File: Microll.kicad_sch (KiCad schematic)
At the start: 3 parts

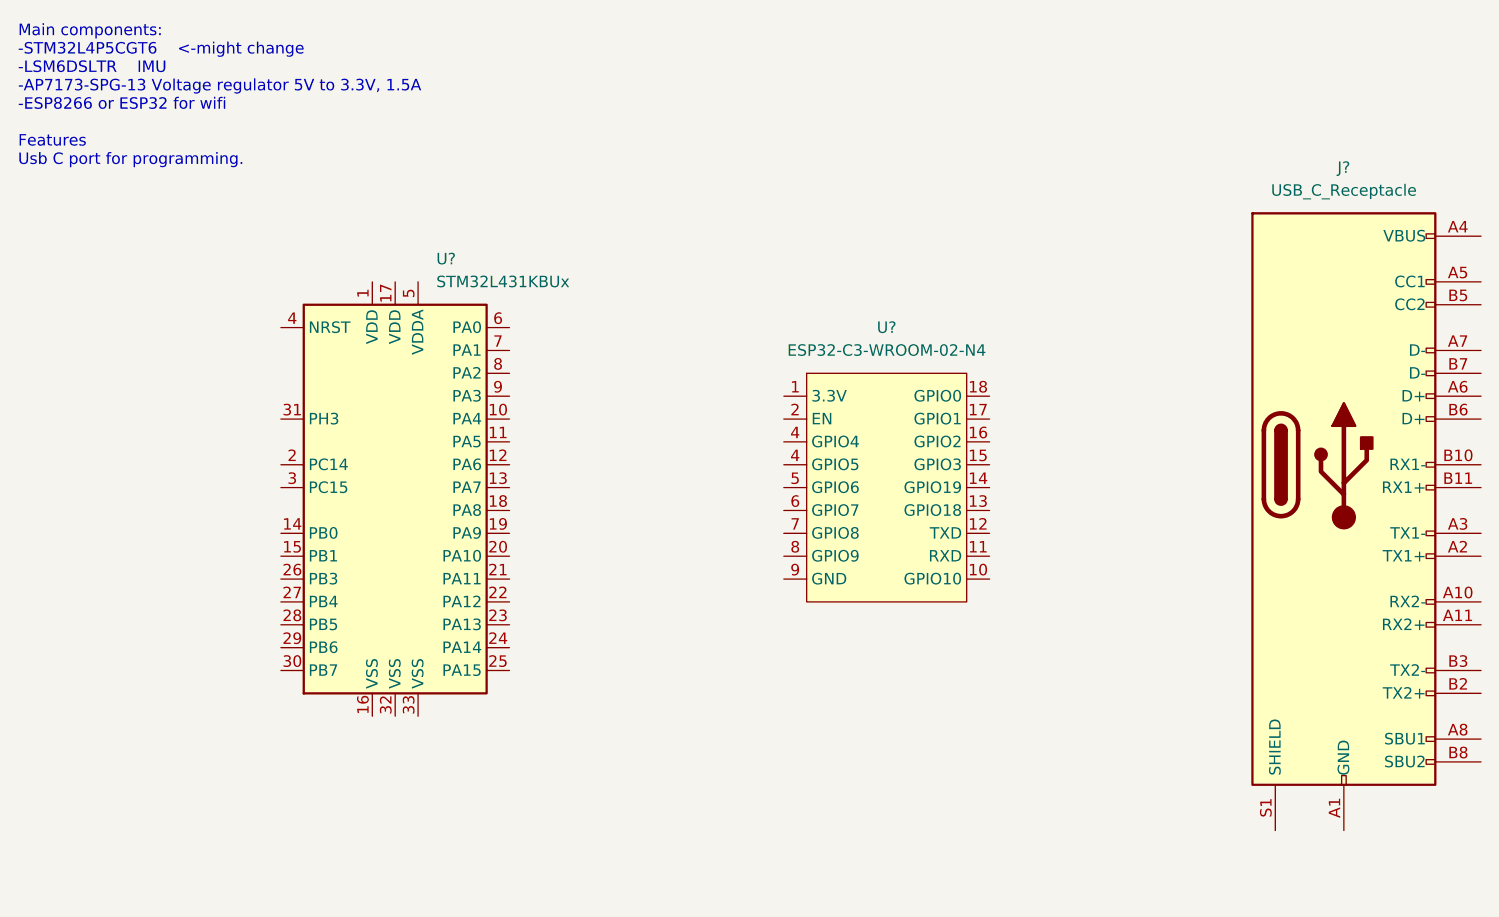
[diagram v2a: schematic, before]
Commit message: Added linear regulator symbol and footprint.
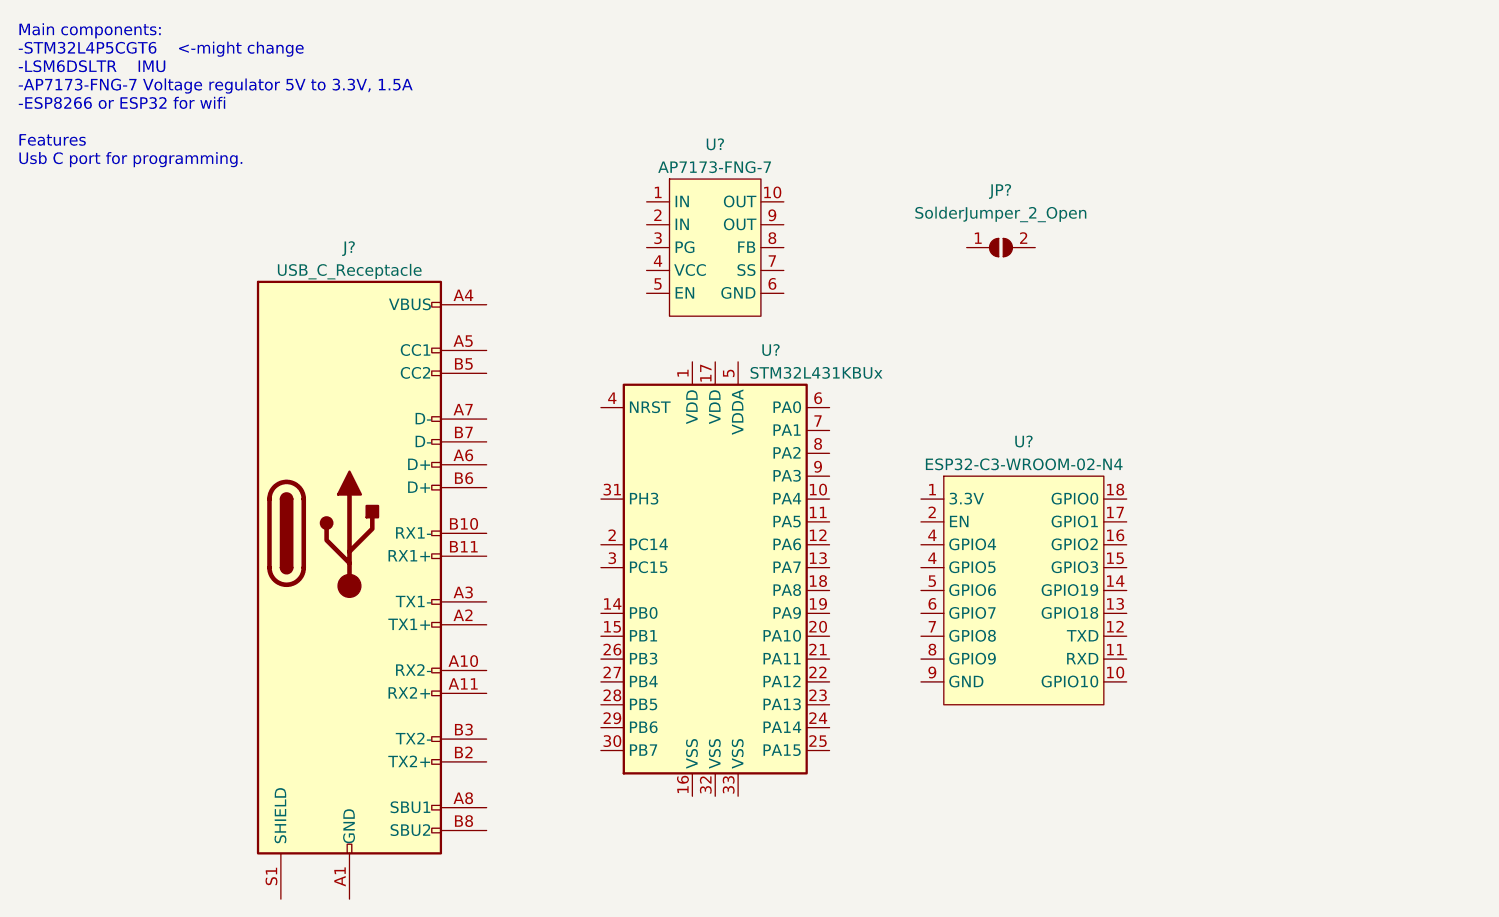
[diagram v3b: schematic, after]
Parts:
- added JP?: SolderJumper_2_Open, symbol Jumper:SolderJumper_2_Open
- added U?: AP7173-FNG-7, AP7173-FNG-7:AP7173-FNG-7, symbol AP7173-FNG-7:AP7173-FNG-7
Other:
- note added: "Main components: -STM32L4P5CGT6 <-might change -LSM6DSLTR IMU -AP7173-FNG-7 Voltage regulator 5V to 3.3V, 1.5A -ESP8266 or ESP32 for wifi Features Usb C port for programming."
- note removed: "Main components: -STM32L4P5CGT6 <-might change -LSM6DSLTR IMU -AP7173-SPG-13 Voltage regulator 5V to 3.3V, 1.5A -ESP8266 or ESP32 for wifi Features Usb C port for programming."
- moved on the sheet: J?, U?
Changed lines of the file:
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@@
 (kicad_sch (version 20211123) (generator eeschema)
   (paper "A4")
-  (text "Main components:\n-STM32L4P5CGT6	<-might change	\n-LSM6DSLTR	IMU\n-AP7173-SPG-13 Voltage regulator 5V to 3.3V, 1.5A\n-ESP8266 or ESP32 for wifi\n\nFeatures\nUsb C port for programming."
+  (text "Main components:\n-STM32L4P5CGT6	<-might change	\n-LSM6DSLTR	IMU\n-AP7173-FNG-7 Voltage regulator 5V to 3.3V, 1.5A\n-ESP8266 or ESP32 for wifi\n\nFeatures\nUsb C port for programming."
     (at 59.69 50.8 0)
     (effects (font (size 1.27 1.27)) (justify left bottom))
   )
-  (symbol (lib_id "MCU_ST_STM32L4:STM32L431KBUx") (at 101.6 86.36 0) (unit 1)
-    (in_bom yes) (on_board yes) (fields_autoplaced)
-    (property "Reference" "U?" (id 0) (at 106.1594 60.96 0)
+  (symbol (lib_id "MCU_ST_STM32L4:STM32L431KBUx") (at 137.16 95.25 0) (unit 1)
+    (in_bom yes) (on_board yes)
+    (property "Reference" "U?" (id 0) (at 142.24 71.12 0)
       (effects (font (size 1.27 1.27)) (justify left))
     )
-    (property "Value" "STM32L431KBUx" (id 1) (at 106.1594 63.5 0)
+    (property "Value" "STM32L431KBUx" (id 1) (at 140.97 73.66 0)
       (effects (font (size 1.27 1.27)) (justify left))
     )
-    (property "Footprint" "Package_DFN_QFN:QFN-32-1EP_5x5mm_P0.5mm_EP3.45x3.45mm" (id 2) (at 91.44 109.22 0)
+    (property "Footprint" "Package_DFN_QFN:QFN-32-1EP_5x5mm_P0.5mm_EP3.45x3.45mm" (id 2) (at 127 118.11 0)
       (effects (font (size 1.27 1.27)) (justify right) hide)
     )
-    (property "Datasheet" "http://www.st.com/st-web-ui/static/active/en/resource/technical/document/datasheet/DM00257211.pdf" (id 3) (at 101.6 86.36 0)
+    (property "Datasheet" "http://www.st.com/st-web-ui/static/active/en/resource/technical/document/datasheet/DM00257211.pdf" (id 3) (at 137.16 95.25 0)
       (effects (font (size 1.27 1.27)) hide)
     )
@@
     (pin "9")
   )
-  (symbol (lib_id "ESP32:ESP32-C3-WROOM-02-N4") (at 156.21 82.55 0) (unit 1)
+  (symbol (lib_id "Jumper:SolderJumper_2_Open") (at 168.91 59.69 0) (unit 1)
     (in_bom yes) (on_board yes) (fields_autoplaced)
-    (property "Reference" "U?" (id 0) (at 156.21 68.58 0))
-    (property "Value" "ESP32-C3-WROOM-02-N4" (id 1) (at 156.21 71.12 0))
-    (property "Footprint" "ESP32:ESP32-C3-WROOM-02-N4" (id 2) (at 156.21 82.55 0)
+    (property "Reference" "JP?" (id 0) (at 168.91 53.34 0))
+    (property "Value" "SolderJumper_2_Open" (id 1) (at 168.91 55.88 0))
+    (property "Footprint" "" (id 2) (at 168.91 59.69 0)
       (effects (font (size 1.27 1.27)) hide)
     )
-    (property "Datasheet" "" (id 3) (at 156.21 82.55 0)
+    (property "Datasheet" "~" (id 3) (at 168.91 59.69 0)
+      (effects (font (size 1.27 1.27)) hide)
+    )
+    (pin "1")
+    (pin "2")
+  )
+  (symbol (lib_id "ESP32:ESP32-C3-WROOM-02-N4") (at 171.45 93.98 0) (unit 1)
+    (in_bom yes) (on_board yes)
+    (property "Reference" "U?" (id 0) (at 171.45 81.28 0))
+    (property "Value" "ESP32-C3-WROOM-02-N4" (id 1) (at 171.45 83.82 0))
+    (property "Footprint" "ESP32:ESP32-C3-WROOM-02-N4" (id 2) (at 171.45 93.98 0)
+      (effects (font (size 1.27 1.27)) hide)
+    )
+    (property "Datasheet" "" (id 3) (at 171.45 93.98 0)
       (effects (font (size 1.27 1.27)) hide)
     )
@@
     (pin "9")
   )
-  (symbol (lib_id "Connector:USB_C_Receptacle") (at 207.01 83.82 0) (unit 1)
-    (in_bom yes) (on_board yes) (fields_autoplaced)
-    (property "Reference" "J?" (id 0) (at 207.01 50.8 0))
-    (property "Value" "USB_C_Receptacle" (id 1) (at 207.01 53.34 0))
-    (property "Footprint" "" (id 2) (at 210.82 83.82 0)
+  (symbol (lib_id "AP7173-FNG-7:AP7173-FNG-7") (at 137.16 57.15 0) (unit 1)
+    (in_bom yes) (on_board yes)
+    (property "Reference" "U?" (id 0) (at 137.16 48.26 0))
+    (property "Value" "AP7173-FNG-7" (id 1) (at 137.16 50.8 0))
+    (property "Footprint" "AP7173-FNG-7:AP7173-FNG-7" (id 2) (at 135.89 57.15 0)
       (effects (font (size 1.27 1.27)) hide)
     )
-    (property "Datasheet" "https://www.usb.org/sites/default/files/documents/usb_type-c.zip" (id 3) (at 210.82 83.82 0)
+    (property "Datasheet" "" (id 3) (at 135.89 57.15 0)
+      (effects (font (size 1.27 1.27)) hide)
+    )
+    (pin "1")
+    (pin "10")
+    (pin "2")
+    (pin "3")
+    (pin "4")
+    (pin "5")
+    (pin "6")
+    (pin "7")
+    (pin "8")
+    (pin "9")
+  )
+  (symbol (lib_id "Connector:USB_C_Receptacle") (at 96.52 91.44 0) (unit 1)
+    (in_bom yes) (on_board yes)
+    (property "Reference" "J?" (id 0) (at 96.52 59.69 0))
+    (property "Value" "USB_C_Receptacle" (id 1) (at 96.52 62.23 0))
+    (property "Footprint" "" (id 2) (at 100.33 91.44 0)
+      (effects (font (size 1.27 1.27)) hide)
+    )
+    (property "Datasheet" "https://www.usb.org/sites/default/files/documents/usb_type-c.zip" (id 3) (at 100.33 91.44 0)
       (effects (font (size 1.27 1.27)) hide)
     )
@@
       (reference "J?") (unit 1) (value "USB_C_Receptacle") (footprint "")
     )
+    (path "/1c3b70c8-9878-40e4-8a0a-63d34ffadd04"
+      (reference "JP?") (unit 1) (value "SolderJumper_2_Open") (footprint "")
+    )
     (path "/086be992-52ad-4b7c-be4a-eeec54e5d292"
       (reference "U?") (unit 1) (value "STM32L431KBUx") (footprint "Package_DFN_QFN:QFN-32-1EP_5x5mm_P0.5mm_EP3.45x3.45mm")
@@
       (reference "U?") (unit 1) (value "ESP32-C3-WROOM-02-N4") (footprint "ESP32:ESP32-C3-WROOM-02-N4")
     )
+    (path "/52ee2e49-a114-4de8-9329-acacfc8b62fc"
+      (reference "U?") (unit 1) (value "AP7173-FNG-7") (footprint "AP7173-FNG-7:AP7173-FNG-7")
+    )
   )

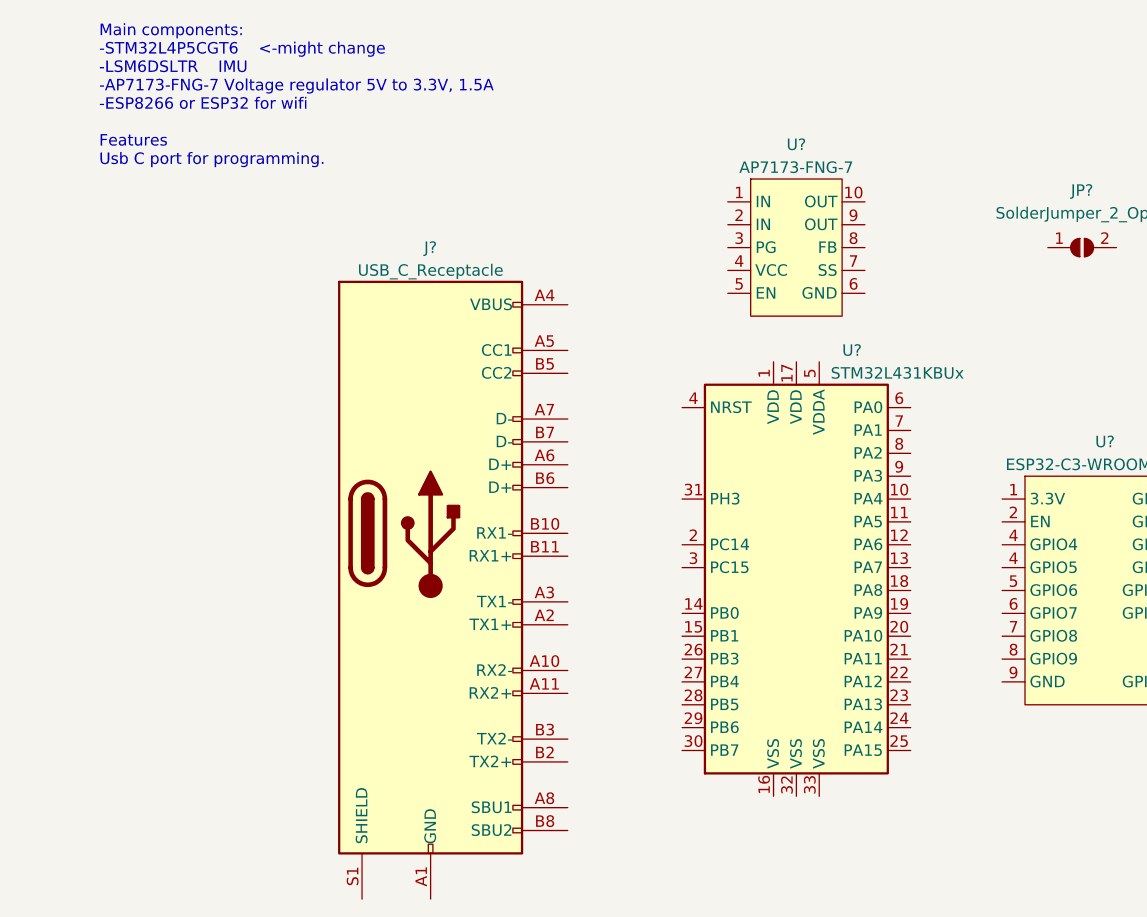
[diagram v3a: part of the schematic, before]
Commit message: Decided on STM32 microcontroller and made footprint and symbol
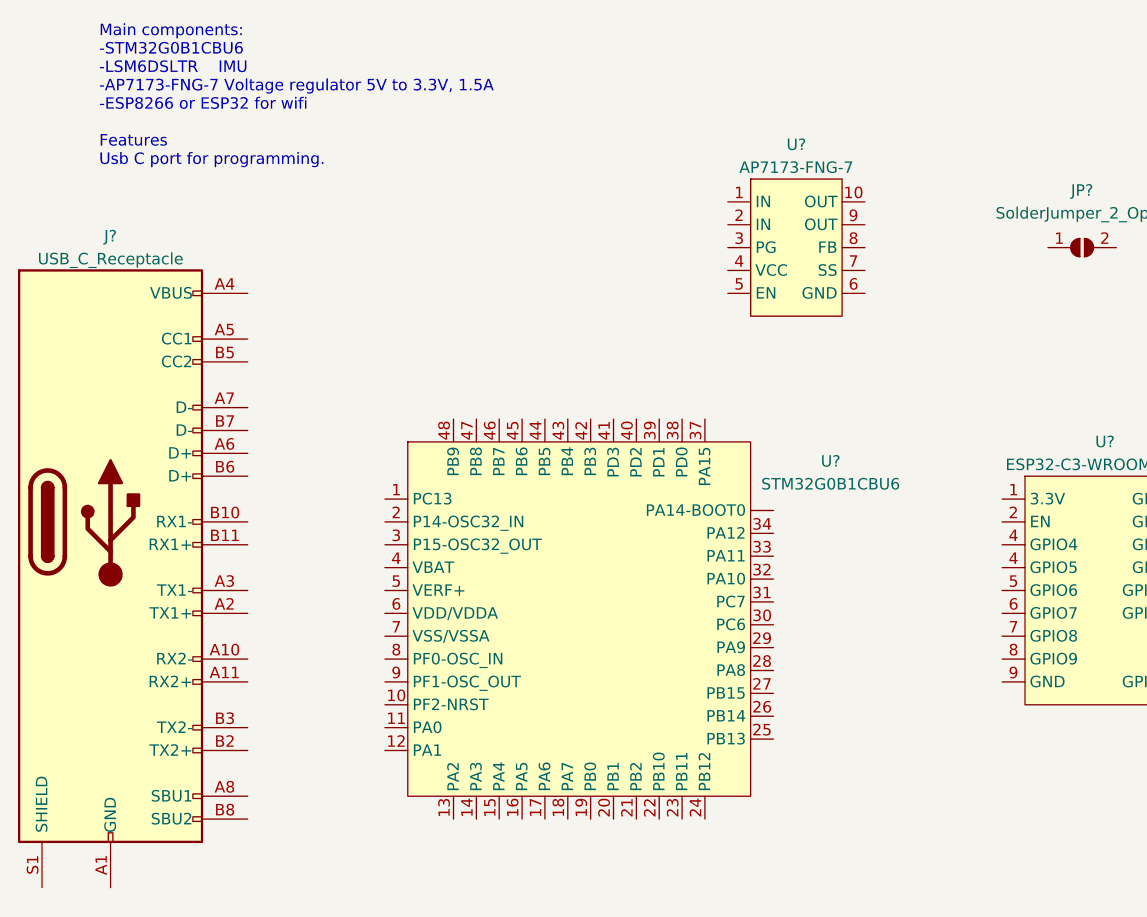
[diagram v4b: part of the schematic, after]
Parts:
- removed U?: STM32L431KBUx, Package_DFN_QFN:QFN-32-1EP_5x5mm_P0.5mm_EP3.45x3.45mm, symbol MCU_ST_STM32L4:STM32L431KBUx
- added U?: STM32G0B1CBU6, STM32:STM32G0B1CBU6, symbol STM32:STM32G0B1CBU6
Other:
- note added: "Main components: -STM32G0B1CBU6 -LSM6DSLTR IMU -AP7173-FNG-7 Voltage regulator 5V to 3.3V, 1.5A -ESP8266 or ESP32 for wifi Features Usb C port for programming."
- note removed: "Main components: -STM32L4P5CGT6 <-might change -LSM6DSLTR IMU -AP7173-FNG-7 Voltage regulator 5V to 3.3V, 1.5A -ESP8266 or ESP32 for wifi Features Usb C port for programming."
- moved on the sheet: J?
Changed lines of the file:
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@@
 (kicad_sch (version 20211123) (generator eeschema)
   (paper "A4")
-  (text "Main components:\n-STM32L4P5CGT6	<-might change	\n-LSM6DSLTR	IMU\n-AP7173-FNG-7 Voltage regulator 5V to 3.3V, 1.5A\n-ESP8266 or ESP32 for wifi\n\nFeatures\nUsb C port for programming."
+  (text "Main components:\n-STM32G0B1CBU6	\n-LSM6DSLTR	IMU\n-AP7173-FNG-7 Voltage regulator 5V to 3.3V, 1.5A\n-ESP8266 or ESP32 for wifi\n\nFeatures\nUsb C port for programming."
     (at 59.69 50.8 0)
     (effects (font (size 1.27 1.27)) (justify left bottom))
-  )
-  (symbol (lib_id "MCU_ST_STM32L4:STM32L431KBUx") (at 137.16 95.25 0) (unit 1)
-    (in_bom yes) (on_board yes)
-    (property "Reference" "U?" (id 0) (at 142.24 71.12 0)
-      (effects (font (size 1.27 1.27)) (justify left))
-    )
-    (property "Value" "STM32L431KBUx" (id 1) (at 140.97 73.66 0)
-      (effects (font (size 1.27 1.27)) (justify left))
-    )
-    (property "Footprint" "Package_DFN_QFN:QFN-32-1EP_5x5mm_P0.5mm_EP3.45x3.45mm" (id 2) (at 127 118.11 0)
-      (effects (font (size 1.27 1.27)) (justify right) hide)
-    )
-    (property "Datasheet" "http://www.st.com/st-web-ui/static/active/en/resource/technical/document/datasheet/DM00257211.pdf" (id 3) (at 137.16 95.25 0)
-      (effects (font (size 1.27 1.27)) hide)
-    )
-    (pin "1")
-    (pin "10")
-    (pin "11")
-    (pin "12")
-    (pin "13")
-    (pin "14")
-    (pin "15")
-    (pin "16")
-    (pin "17")
-    (pin "18")
-    (pin "19")
-    (pin "2")
-    (pin "20")
-    (pin "21")
-    (pin "22")
-    (pin "23")
-    (pin "24")
-    (pin "25")
-    (pin "26")
-    (pin "27")
-    (pin "28")
-    (pin "29")
-    (pin "3")
-    (pin "30")
-    (pin "31")
-    (pin "32")
-    (pin "33")
-    (pin "4")
-    (pin "5")
-    (pin "6")
-    (pin "7")
-    (pin "8")
-    (pin "9")
   )
   (symbol (lib_id "Jumper:SolderJumper_2_Open") (at 168.91 59.69 0) (unit 1)
@@
     (pin "9")
   )
+  (symbol (lib_id "STM32:STM32G0B1CBU6") (at 113.03 101.6 0) (unit 1)
+    (in_bom yes) (on_board yes) (fields_autoplaced)
+    (property "Reference" "U?" (id 0) (at 140.97 83.4388 0))
+    (property "Value" "STM32G0B1CBU6" (id 1) (at 140.97 85.9788 0))
+    (property "Footprint" "STM32:STM32G0B1CBU6" (id 2) (at 105.41 92.71 0)
+      (effects (font (size 1.27 1.27)) hide)
+    )
+    (property "Datasheet" "" (id 3) (at 105.41 92.71 0)
+      (effects (font (size 1.27 1.27)) hide)
+    )
+    (pin "")
+    (pin "1")
+    (pin "10")
+    (pin "11")
+    (pin "12")
+    (pin "13")
+    (pin "14")
+    (pin "15")
+    (pin "16")
+    (pin "17")
+    (pin "18")
+    (pin "19")
+    (pin "2")
+    (pin "20")
+    (pin "21")
+    (pin "22")
+    (pin "23")
+    (pin "24")
+    (pin "25")
+    (pin "26")
+    (pin "27")
+    (pin "28")
+    (pin "29")
+    (pin "3")
+    (pin "30")
+    (pin "31")
+    (pin "32")
+    (pin "33")
+    (pin "34")
+    (pin "37")
+    (pin "38")
+    (pin "39")
+    (pin "4")
+    (pin "40")
+    (pin "41")
+    (pin "42")
+    (pin "43")
+    (pin "44")
+    (pin "45")
+    (pin "46")
+    (pin "47")
+    (pin "48")
+    (pin "5")
+    (pin "6")
+    (pin "7")
+    (pin "8")
+    (pin "9")
+  )
   (symbol (lib_id "AP7173-FNG-7:AP7173-FNG-7") (at 137.16 57.15 0) (unit 1)
     (in_bom yes) (on_board yes)
@@
     (pin "9")
   )
-  (symbol (lib_id "Connector:USB_C_Receptacle") (at 96.52 91.44 0) (unit 1)
+  (symbol (lib_id "Connector:USB_C_Receptacle") (at 60.96 90.17 0) (unit 1)
     (in_bom yes) (on_board yes)
-    (property "Reference" "J?" (id 0) (at 96.52 59.69 0))
-    (property "Value" "USB_C_Receptacle" (id 1) (at 96.52 62.23 0))
-    (property "Footprint" "" (id 2) (at 100.33 91.44 0)
+    (property "Reference" "J?" (id 0) (at 60.96 58.42 0))
+    (property "Value" "USB_C_Receptacle" (id 1) (at 60.96 60.96 0))
+    (property "Footprint" "" (id 2) (at 64.77 90.17 0)
       (effects (font (size 1.27 1.27)) hide)
     )
-    (property "Datasheet" "https://www.usb.org/sites/default/files/documents/usb_type-c.zip" (id 3) (at 100.33 91.44 0)
+    (property "Datasheet" "https://www.usb.org/sites/default/files/documents/usb_type-c.zip" (id 3) (at 64.77 90.17 0)
       (effects (font (size 1.27 1.27)) hide)
     )
@@
       (reference "JP?") (unit 1) (value "SolderJumper_2_Open") (footprint "")
     )
-    (path "/086be992-52ad-4b7c-be4a-eeec54e5d292"
-      (reference "U?") (unit 1) (value "STM32L431KBUx") (footprint "Package_DFN_QFN:QFN-32-1EP_5x5mm_P0.5mm_EP3.45x3.45mm")
-    )
     (path "/3757d3b5-a25c-4772-93e2-fe7135fc4c50"
       (reference "U?") (unit 1) (value "ESP32-C3-WROOM-02-N4") (footprint "ESP32:ESP32-C3-WROOM-02-N4")
     )
+    (path "/5002f28f-3ca0-40e2-85f9-0c282d89806e"
+      (reference "U?") (unit 1) (value "STM32G0B1CBU6") (footprint "STM32:STM32G0B1CBU6")
+    )
     (path "/52ee2e49-a114-4de8-9329-acacfc8b62fc"
